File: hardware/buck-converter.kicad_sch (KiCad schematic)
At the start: 1 part

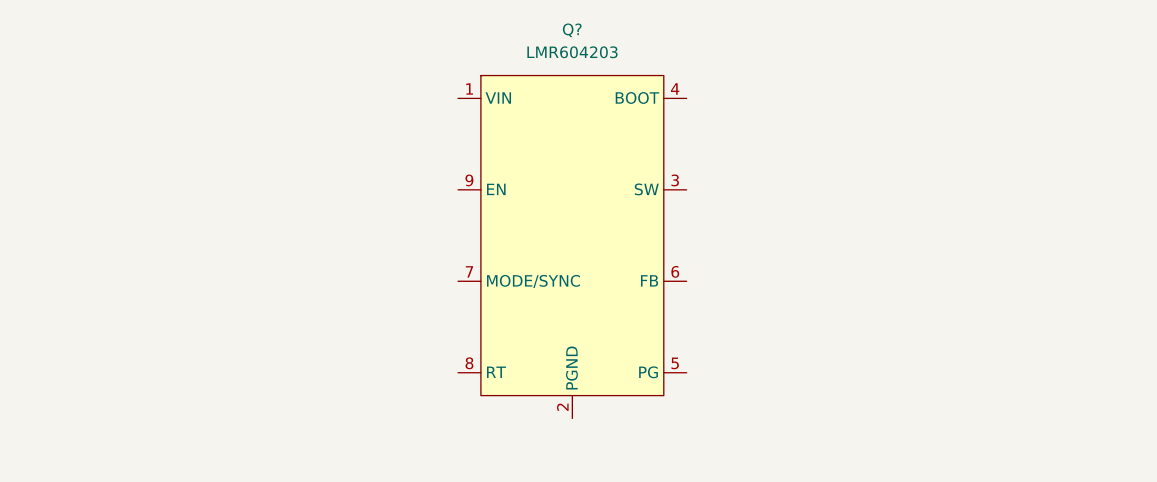
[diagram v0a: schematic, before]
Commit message: Add 3.3V buck converter
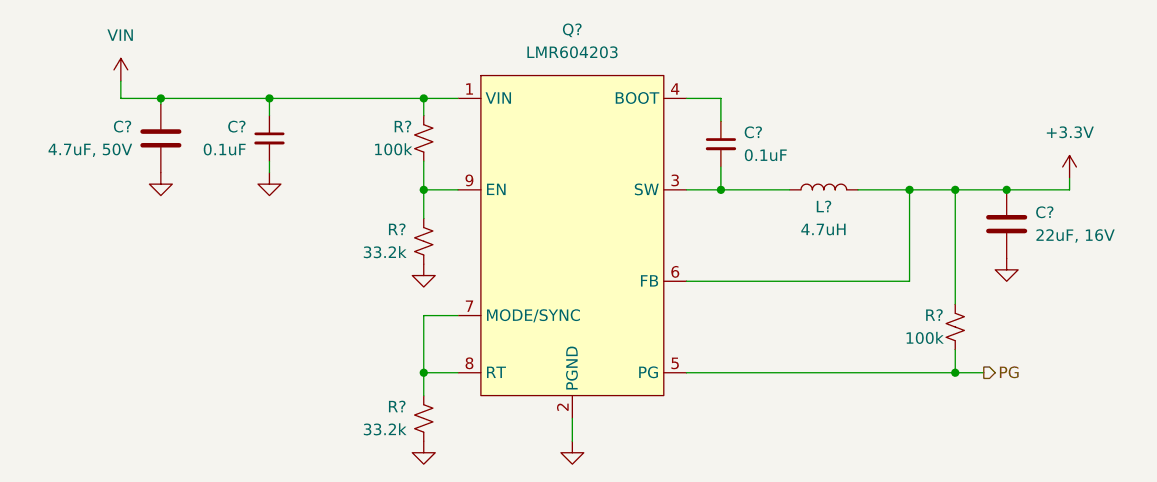
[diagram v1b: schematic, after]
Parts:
- added C? (x2): 0.1uF, Capacitor_SMD:C_0603_1608Metric_Pad1.08x0.95mm_HandSolder, symbol Device:C_Small
- added C?: 22uF, 16V, Capacitor_SMD:C_1210_3225Metric_Pad1.33x2.70mm_HandSolder, symbol Device:C
- added C?: 4.7uF, 50V, Capacitor_SMD:C_1206_3216Metric_Pad1.33x1.80mm_HandSolder, symbol Device:C
- added L?: 4.7uH, Inductor_SMD:L_Chilisin_BMRB00050518-B, symbol Device:L
- added R? (x2): 33.2k, Resistor_SMD:R_0603_1608Metric_Pad0.98x0.95mm_HandSolder, symbol Device:R_Small_US
- added R? (x2): 100k, Resistor_SMD:R_0603_1608Metric_Pad0.98x0.95mm_HandSolder, symbol Device:R_Small_US
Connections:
- net VIN: now reaches Q?.1 (VIN)
- net VIN: now also C?.1, C?.1, R?.1
- net GND: now reaches Q?.2 (PGND)
- net GND: now also C?.2, C?.2, C?.2, R?.2, R?.2
- net at Q?.3 (SW): now also C?.2, L?.1
- net at Q?.4 (BOOT): now also C?.1
- net PG: now reaches Q?.5 (PG)
- net PG: now also R?.2
- net +3.3V: now reaches Q?.6 (FB)
- net +3.3V: now also C?.1, L?.2, R?.1
- net at Q?.7 (MODE/SYNC): now also Q?.8 (RT), R?.1
- net at Q?.9 (EN): now also R?.1, R?.2

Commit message: Create MCU schematic
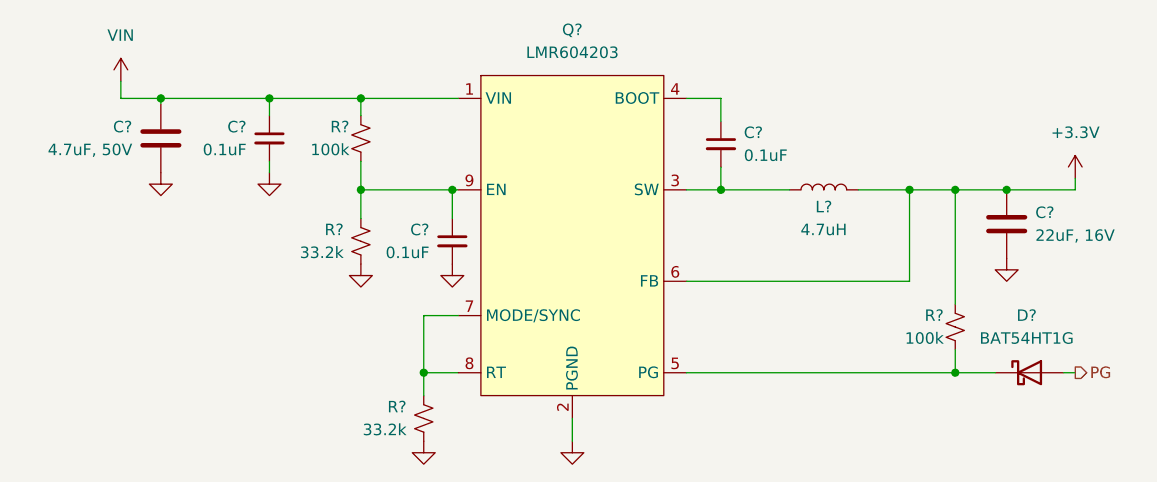
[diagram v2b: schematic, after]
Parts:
- added C?: 0.1uF, Capacitor_SMD:C_0603_1608Metric_Pad1.08x0.95mm_HandSolder, symbol Device:C_Small
- added D?: BAT54HT1G, Diode_SMD:D_SOD-323, symbol Device:D_Schottky
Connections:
- net GND: now also C?.2
- net PG: now also D?.2 (A); no longer Q?.5 (PG), R?.2
- net at Q?.9 (EN), R?.1, R?.2: now also C?.1
- new net: D?.1 (K), Q?.5 (PG), R?.2
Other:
- company: (none) -> Jacob Wigent
- title: (none) -> 3.3V Buck Converter
- moved on the sheet: R?
